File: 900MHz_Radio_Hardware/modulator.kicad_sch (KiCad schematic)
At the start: 6 parts

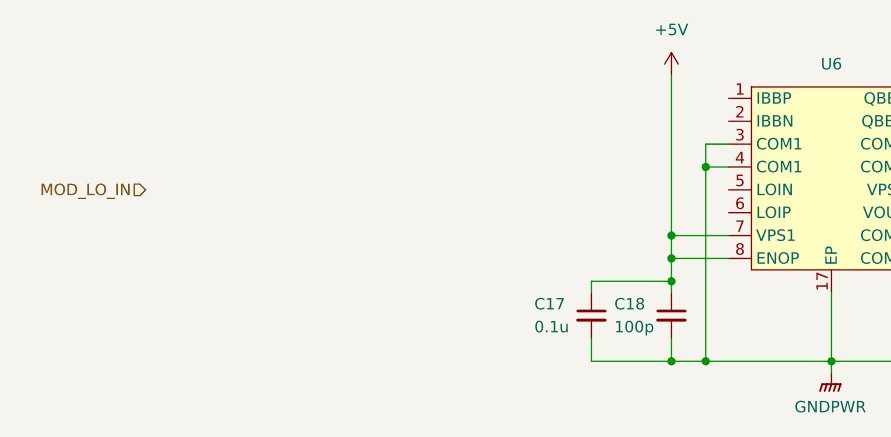
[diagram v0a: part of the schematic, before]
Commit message: Added balun to modulator
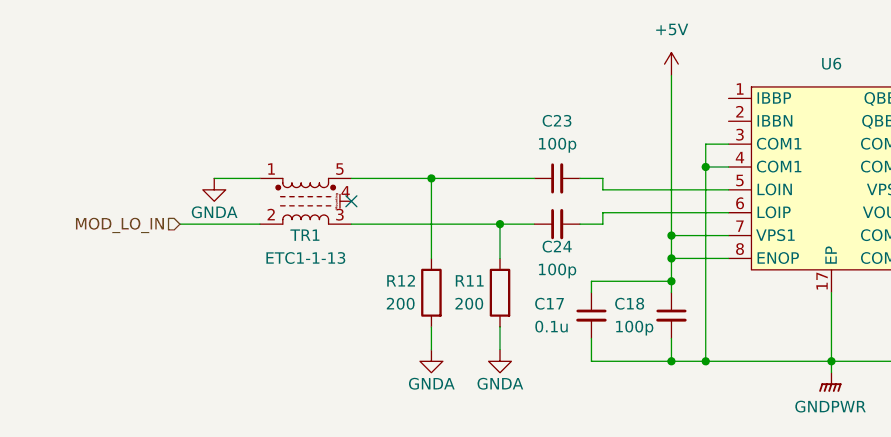
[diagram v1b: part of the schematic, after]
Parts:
- added C23, C24: 100p, symbol Device:C_Small
- added R11, R12: 200, symbol Device:R
- added TR1: ETC1-1-13, Transformer_SMD:Transformer_MACOM_SM-22, symbol Transformer:ETC1-1-13
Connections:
- net MOD_LO_IN: now also TR1.2
- net at U6.5 (LOIN): now also C23.2
- net at U6.6 (LOIP): now also C24.2
- new net: C23.1, R12.1, TR1.5
- new net: C24.1, R11.1, TR1.3
- new net GNDA: R11.2, R12.2, TR1.1
- no-connect marks 0 -> 1

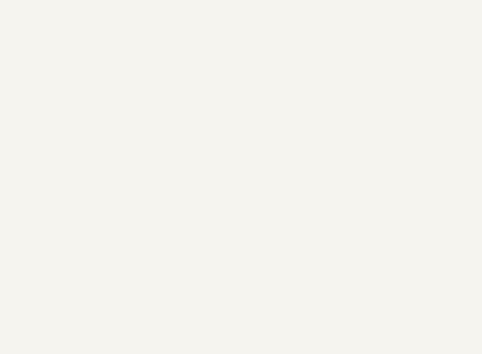
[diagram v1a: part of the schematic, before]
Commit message: Hardware for IQ signal synchronization
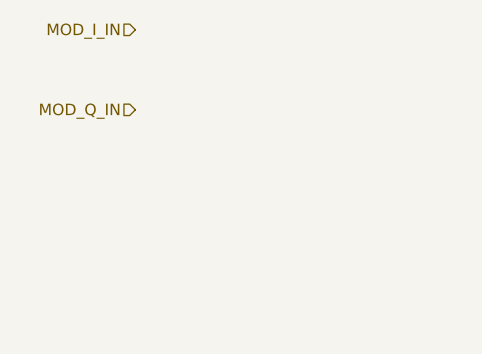
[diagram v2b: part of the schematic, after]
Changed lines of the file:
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@@
     (effects (font (size 1.27 1.27)) (justify left))
+  )
+  (hierarchical_label "MOD_Q_IN" (shape input) (at 29.21 33.02 180) (fields_autoplaced)
+    (effects (font (size 1.27 1.27)) (justify right))
+  )
+  (hierarchical_label "MOD_I_IN" (shape input) (at 29.21 24.13 180) (fields_autoplaced)
+    (effects (font (size 1.27 1.27)) (justify right))
   )
   (symbol (lib_id "Device:R") (at 101.6 100.33 0) (mirror y) (unit 1)

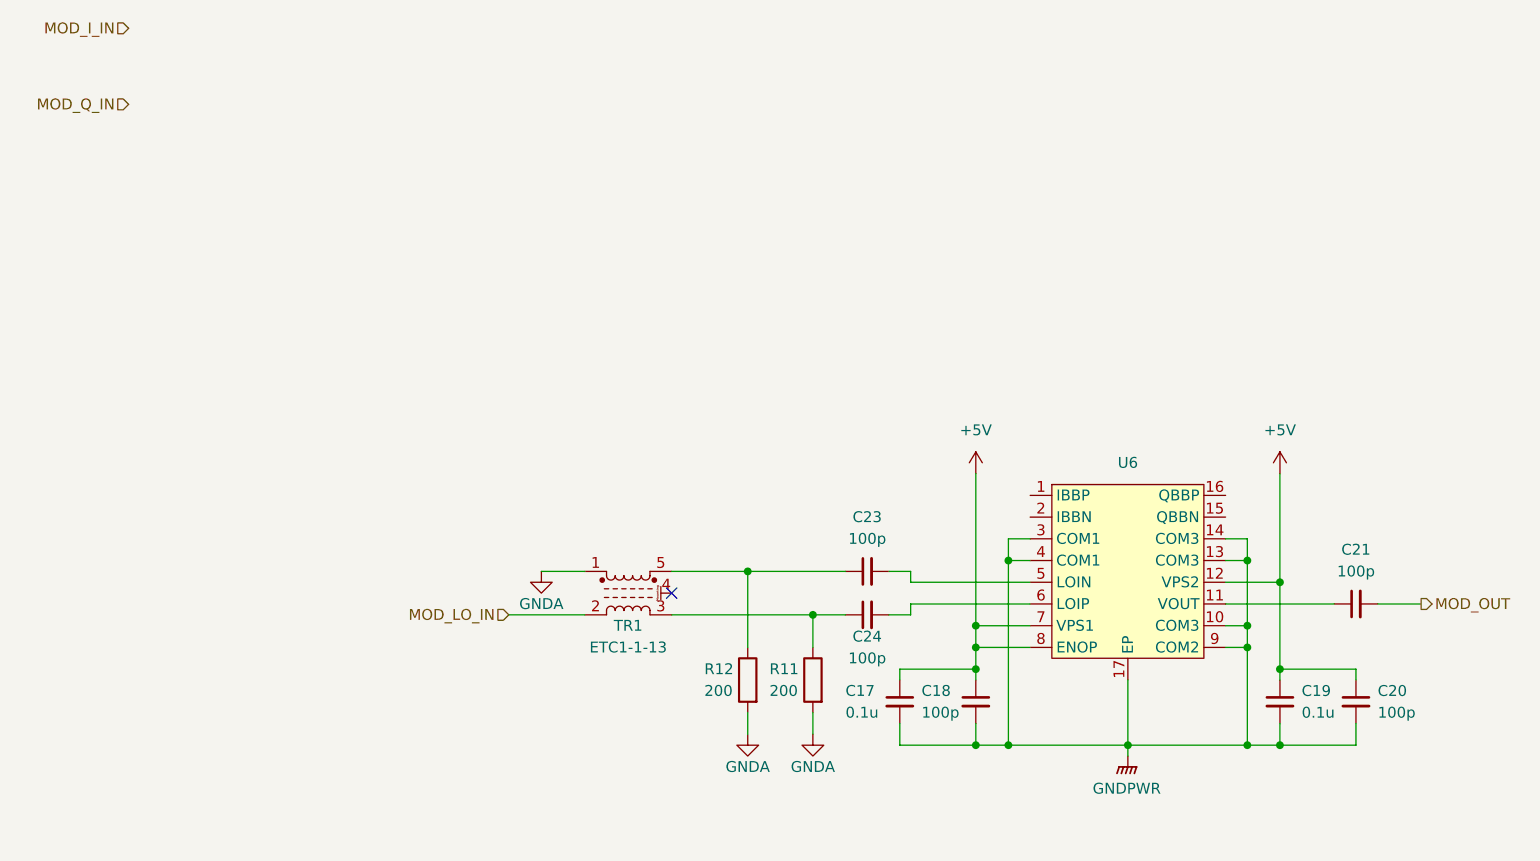
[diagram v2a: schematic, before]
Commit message: Added modulator enable signal
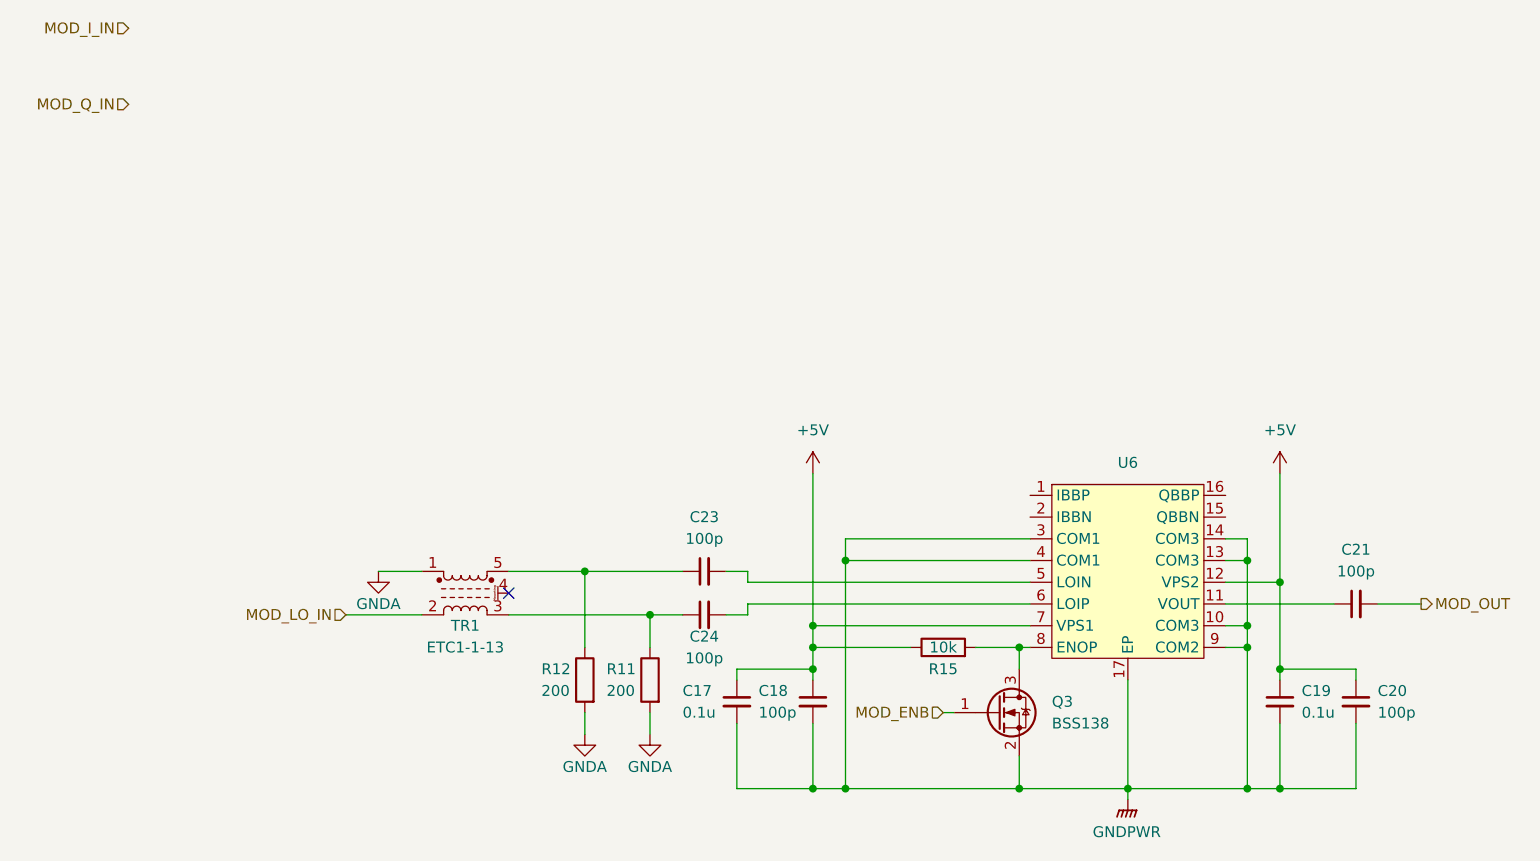
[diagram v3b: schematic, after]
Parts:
- added Q3: BSS138, Package_TO_SOT_SMD:SOT-23, symbol Transistor_FET:BSS138
- added R15: 10k, symbol Device:R
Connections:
- net +5V: now also R15.1; no longer U6.8 (ENOP)
- net GNDPWR: now also Q3.2 (S)
- new net: Q3.3 (D), R15.2, U6.8 (ENOP)
- new net MOD_ENB: Q3.1 (G)
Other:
- moved on the sheet: C17, C18, C23, C24, R11, R12, TR1

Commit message: Replaced DAC
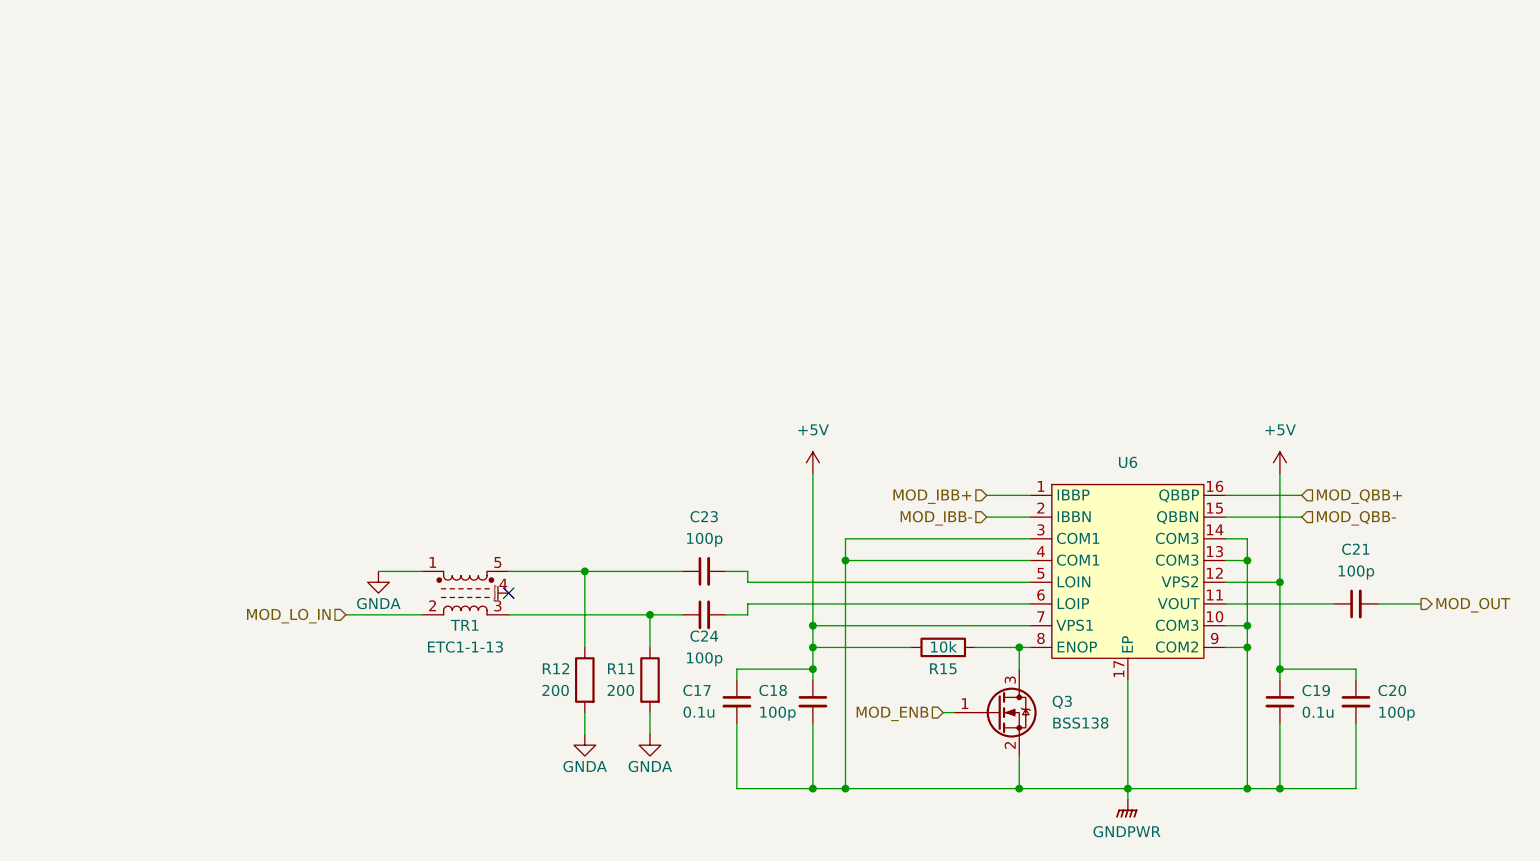
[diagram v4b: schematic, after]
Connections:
- net MOD_IBB+: now reaches U6.1 (IBBP)
- net MOD_QBB-: now reaches U6.15 (QBBN)
- net MOD_QBB+: now reaches U6.16 (QBBP)
- net MOD_IBB-: now reaches U6.2 (IBBN)
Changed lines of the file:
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@@
+    (stroke (width 0) (type default))
+  )
+  (wire (pts (xy 129.54 78.74) (xy 134.62 78.74))
     (stroke (width 0) (type default))
   )
@@
     (stroke (width 0) (type default))
   )
+  (wire (pts (xy 157.48 78.74) (xy 166.37 78.74))
+    (stroke (width 0) (type default))
+  )
   (wire (pts (xy 73.66 87.63) (xy 82.55 87.63))
     (stroke (width 0) (type default))
@@
     (stroke (width 0) (type default))
   )
+  (wire (pts (xy 129.54 81.28) (xy 134.62 81.28))
+    (stroke (width 0) (type default))
+  )
   (wire (pts (xy 134.62 88.9) (xy 101.6 88.9))
     (stroke (width 0) (type default))
@@
     (stroke (width 0) (type default))
   )
+  (wire (pts (xy 157.48 81.28) (xy 166.37 81.28))
+    (stroke (width 0) (type default))
+  )
   (wire (pts (xy 160.02 93.98) (xy 157.48 93.98))
     (stroke (width 0) (type default))
@@
     (stroke (width 0) (type default))
   )
+  (hierarchical_label "MOD_QBB+" (shape input) (at 166.37 78.74 0) (fields_autoplaced)
+    (effects (font (size 1.27 1.27)) (justify left))
+  )
   (hierarchical_label "MOD_ENB" (shape input) (at 124.46 104.14 180) (fields_autoplaced)
     (effects (font (size 1.27 1.27)) (justify right))
+  )
+  (hierarchical_label "MOD_IBB+" (shape input) (at 129.54 78.74 180) (fields_autoplaced)
+    (effects (font (size 1.27 1.27)) (justify right))
+  )
+  (hierarchical_label "MOD_IBB-" (shape input) (at 129.54 81.28 180) (fields_autoplaced)
+    (effects (font (size 1.27 1.27)) (justify right))
+  )
+  (hierarchical_label "MOD_QBB-" (shape input) (at 166.37 81.28 0) (fields_autoplaced)
+    (effects (font (size 1.27 1.27)) (justify left))
   )
   (hierarchical_label "MOD_LO_IN" (shape input) (at 54.61 92.71 180) (fields_autoplaced)
@@
     (effects (font (size 1.27 1.27)) (justify left))
   )
-  (hierarchical_label "MOD_Q_IN" (shape input) (at 29.21 33.02 180) (fields_autoplaced)
-    (effects (font (size 1.27 1.27)) (justify right))
-  )
-  (hierarchical_label "MOD_I_IN" (shape input) (at 29.21 24.13 180) (fields_autoplaced)
-    (effects (font (size 1.27 1.27)) (justify right))
-  )
   (symbol (lib_id "Device:R") (at 82.55 100.33 0) (mirror y) (unit 1)
